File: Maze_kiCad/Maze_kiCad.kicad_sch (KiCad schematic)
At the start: 1 part, among them U1 ESP32-S2-DevKitC-1

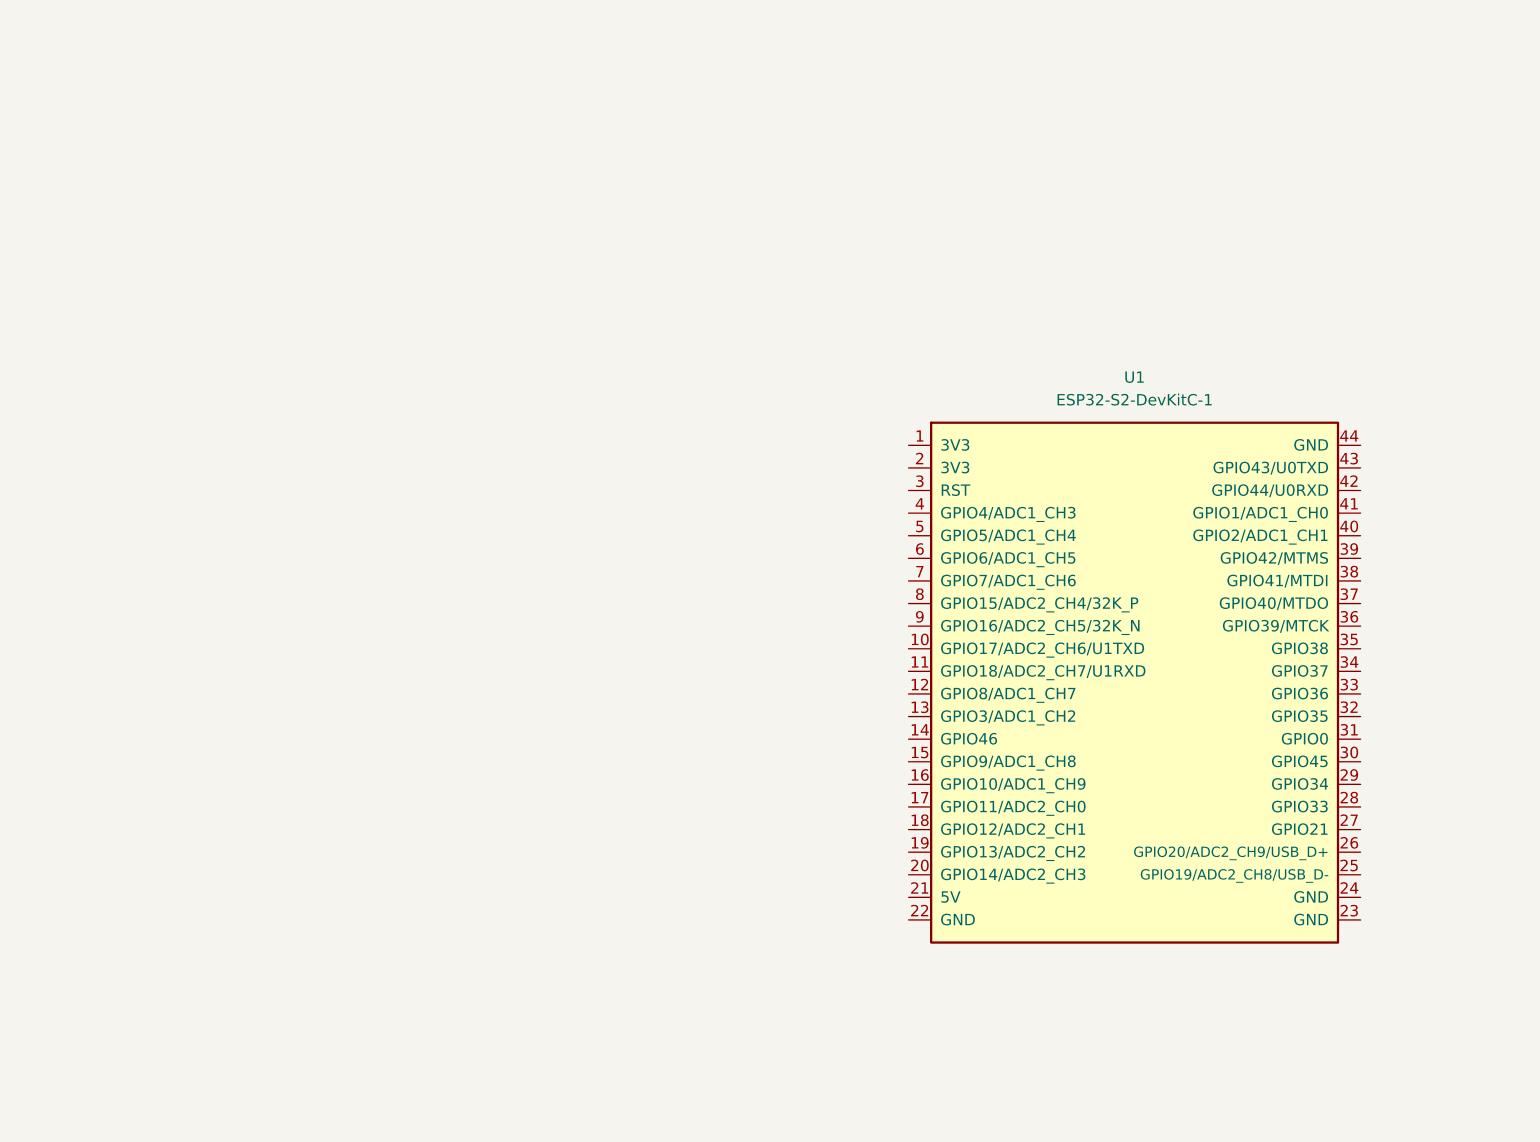
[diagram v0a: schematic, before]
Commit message: Add ir sensor
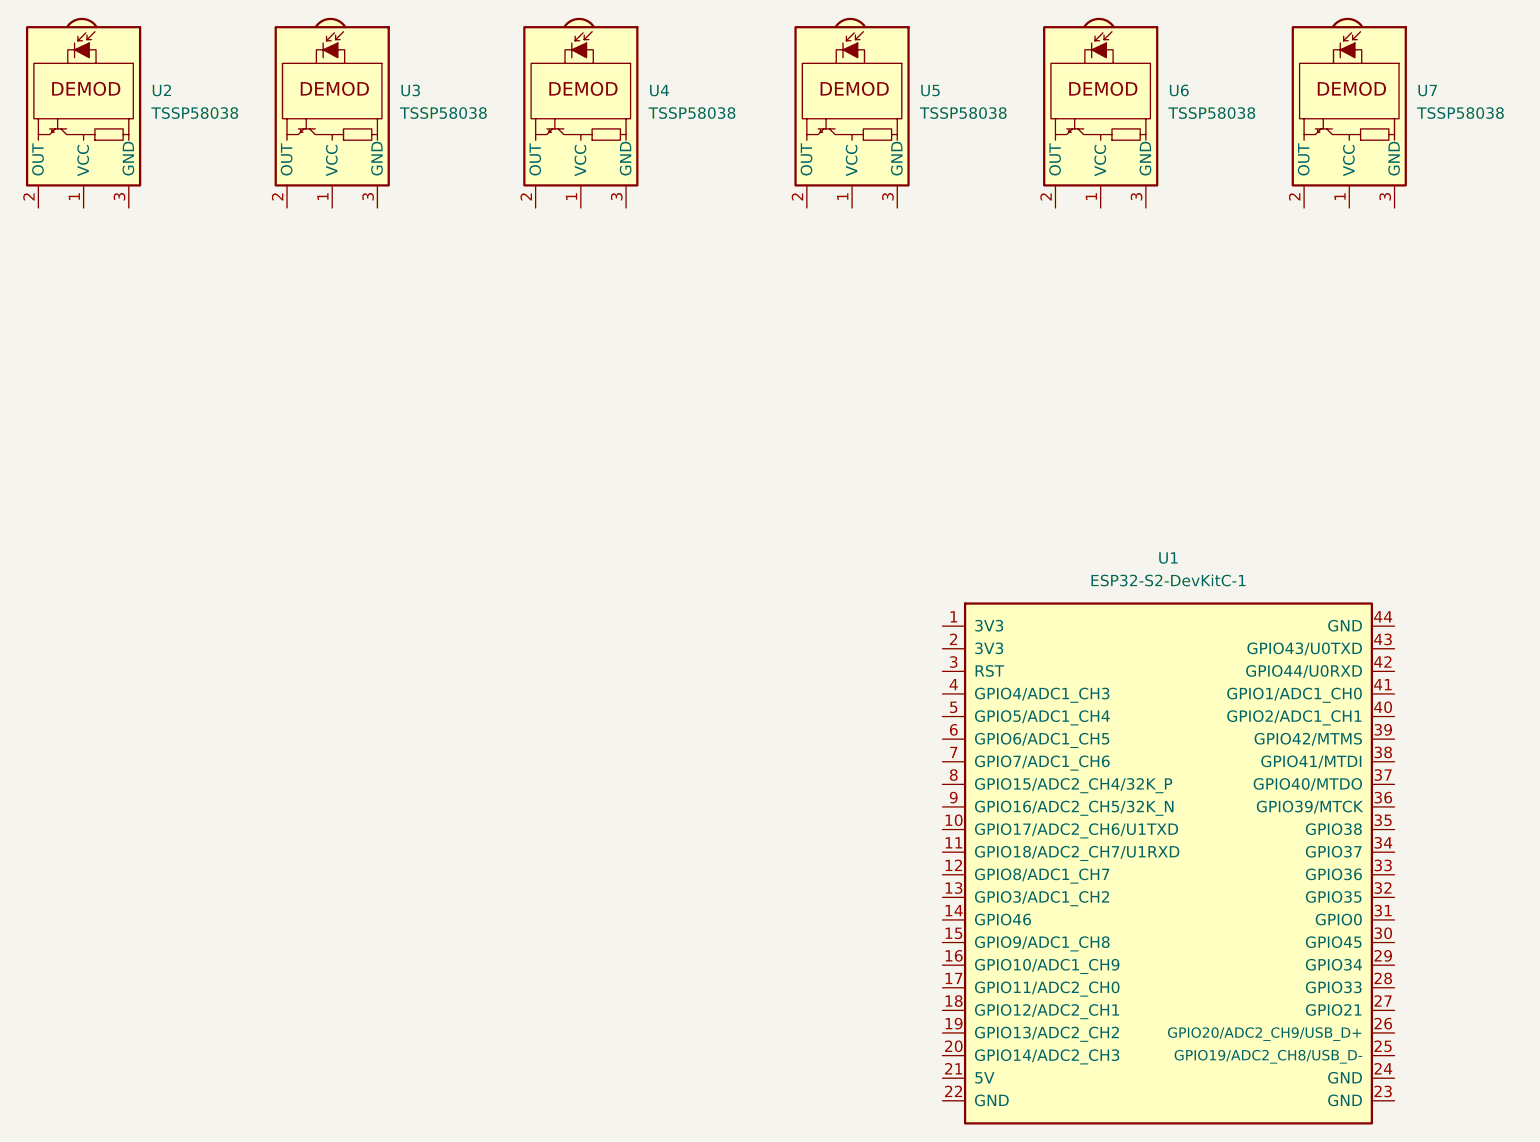
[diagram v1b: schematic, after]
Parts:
- added U2, U3, U4, U5, U6, U7: TSSP58038, OptoDevice:Vishay_MINICAST-3Pin, symbol Sensor_Proximity:TSSP58038
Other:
- moved on the sheet: U1

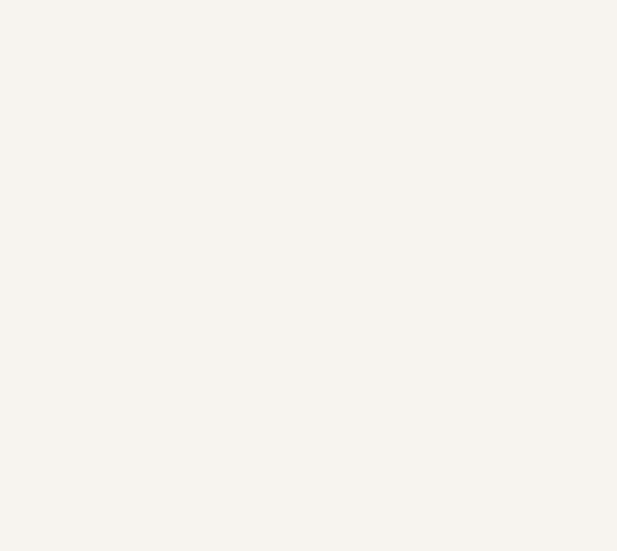
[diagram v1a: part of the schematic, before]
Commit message: add gyroscope symbol-footprint
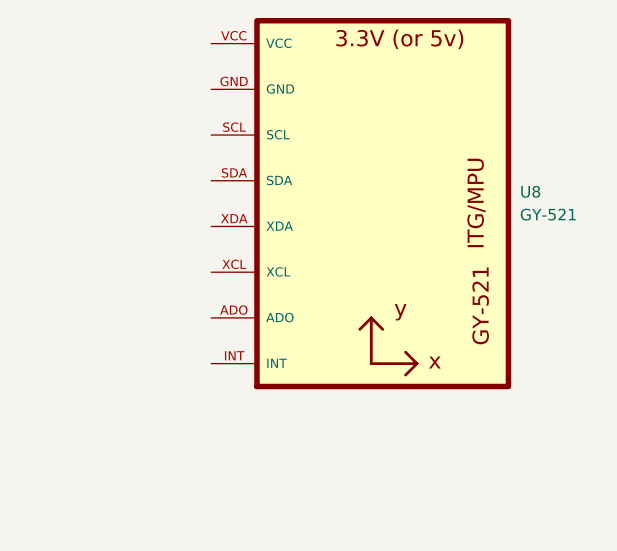
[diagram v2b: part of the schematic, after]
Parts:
- added U8: GY-521, mpu6050:GY-521, symbol mpu6050:GY-521
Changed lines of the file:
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@@
+	)
+	(symbol
+		(lib_id "mpu6050:GY-521")
+		(at 255.27 35.56 0)
+		(unit 1)
+		(exclude_from_sim no)
+		(in_bom yes)
+		(on_board yes)
+		(dnp no)
+		(fields_autoplaced yes)
+		(property "Reference" "U8"
+			(at 274.32 36.8299 0)
+			(effects
+				(font
+					(size 1.27 1.27)
+				)
+				(justify left)
+			)
+		)
+		(property "Value" "GY-521"
+			(at 274.32 39.3699 0)
+			(effects
+				(font
+					(size 1.27 1.27)
+				)
+				(justify left)
+			)
+		)
+		(property "Footprint" "mpu6050:GY-521"
+			(at 255.27 35.56 0)
+			(effects
+				(font
+					(size 1.27 1.27)
+				)
+				(justify bottom)
+				(hide yes)
+			)
+		)
+		(property "Datasheet" ""
+			(at 255.27 35.56 0)
+			(effects
+				(font
+					(size 1.27 1.27)
+				)
+				(hide yes)
+			)
+		)
+		(property "Description" ""
+			(at 255.27 35.56 0)
+			(effects
+				(font
+					(size 1.27 1.27)
+				)
+				(hide yes)
+			)
+		)
+		(property "MF" "GODREAM FORDREAM CO., LIMITED"
+			(at 255.27 35.56 0)
+			(effects
+				(font
+					(size 1.27 1.27)
+				)
+				(justify bottom)
+				(hide yes)
+			)
+		)
+		(property "Description_1" "\nTriple Axis Accelerometer Gyro Breakout\n"
+			(at 255.27 35.56 0)
+			(effects
+				(font
+					(size 1.27 1.27)
+				)
+				(justify bottom)
+				(hide yes)
+			)
+		)
+		(property "Package" "Package"
+			(at 255.27 35.56 0)
+			(effects
+				(font
+					(size 1.27 1.27)
+				)
+				(justify bottom)
+				(hide yes)
+			)
+		)
+		(property "Price" "None"
+			(at 255.27 35.56 0)
+			(effects
+				(font
+					(size 1.27 1.27)
+				)
+				(justify bottom)
+				(hide yes)
+			)
+		)
+		(property "SnapEDA_Link" "https://www.snapeda.com/parts/GY-521/GODREAM+FORDREAM+CO.%252C+LIMITED/view-part/?ref=snap"
+			(at 255.27 35.56 0)
+			(effects
+				(font
+					(size 1.27 1.27)
+				)
+				(justify bottom)
+				(hide yes)
+			)
+		)
+		(property "MP" "GY-521"
+			(at 255.27 35.56 0)
+			(effects
+				(font
+					(size 1.27 1.27)
+				)
+				(justify bottom)
+				(hide yes)
+			)
+		)
+		(property "Availability" "Not in stock"
+			(at 255.27 35.56 0)
+			(effects
+				(font
+					(size 1.27 1.27)
+				)
+				(justify bottom)
+				(hide yes)
+			)
+		)
+		(property "Check_prices" "https://www.snapeda.com/parts/GY-521/GODREAM+FORDREAM+CO.%252C+LIMITED/view-part/?ref=eda"
+			(at 255.27 35.56 0)
+			(effects
+				(font
+					(size 1.27 1.27)
+				)
+				(justify bottom)
+				(hide yes)
+			)
+		)
+		(pin "SCL"
+		)
+		(pin "INT"
+		)
+		(pin "XDA"
+		)
+		(pin "GND"
+		)
+		(pin "SDA"
+		)
+		(pin "XCL"
+		)
+		(pin "ADO"
+		)
+		(pin "VCC"
+		)
+		(instances
+			(project "Maze_kiCad"
+				(path "/22108416-3e7d-4108-b707-2b088264c2dd"
+					(reference "U8")
+					(unit 1)
+				)
+			)
+		)
 	)
 	(symbol

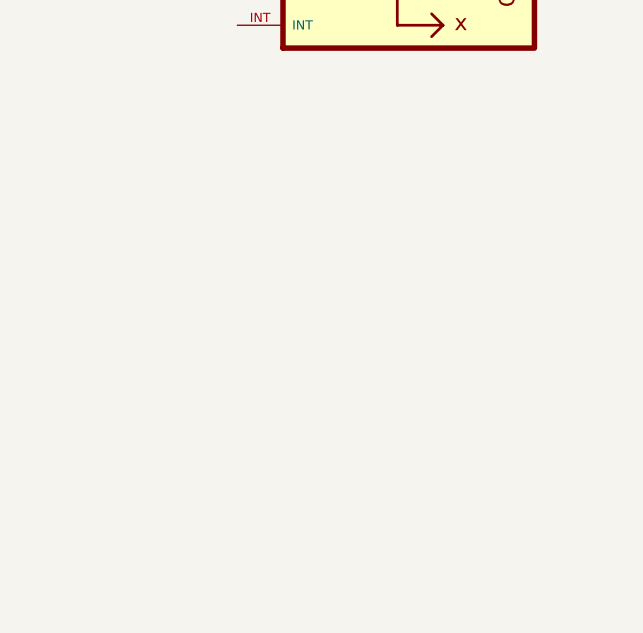
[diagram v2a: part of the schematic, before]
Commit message: drv8835 motor driver symnol and footprint
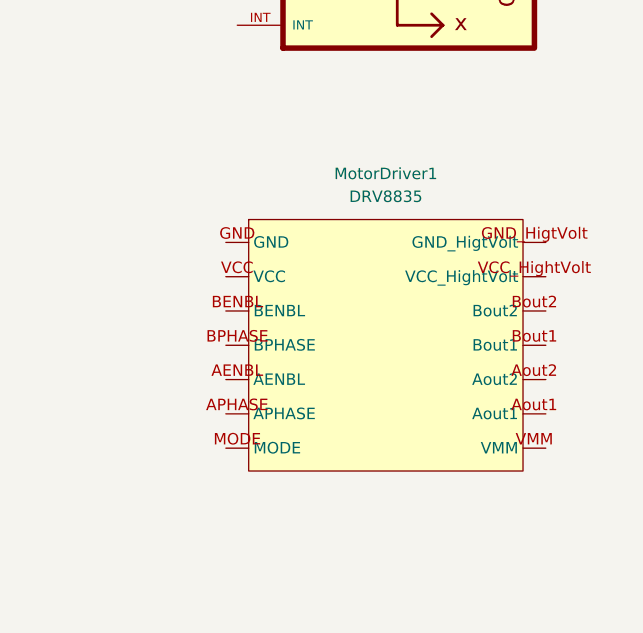
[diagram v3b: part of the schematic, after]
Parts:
- added MotorDriver1: DRV8835, drv8835:drv8835, symbol drv8835:DRV8835
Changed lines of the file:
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@@
+	)
+	(symbol
+		(lib_id "drv8835:DRV8835")
+		(at 284.48 69.85 0)
+		(unit 1)
+		(exclude_from_sim no)
+		(in_bom yes)
+		(on_board yes)
+		(dnp no)
+		(fields_autoplaced yes)
+		(property "Reference" "MotorDriver1"
+			(at 256.54 72.39 0)
+			(effects
+				(font
+					(size 1.27 1.27)
+				)
+			)
+		)
+		(property "Value" "DRV8835"
+			(at 256.54 74.93 0)
+			(effects
+				(font
+					(size 1.27 1.27)
+				)
+			)
+		)
+		(property "Footprint" "drv8835:drv8835"
+			(at 256.54 92.71 0)
+			(effects
+				(font
+					(size 1.27 1.27)
+				)
+				(hide yes)
+			)
+		)
+		(property "Datasheet" ""
+			(at 256.54 92.71 0)
+			(effects
+				(font
+					(size 1.27 1.27)
+				)
+				(hide yes)
+			)
+		)
+		(property "Description" ""
+			(at 256.54 92.71 0)
+			(effects
+				(font
+					(size 1.27 1.27)
+				)
+				(hide yes)
+			)
+		)
+		(pin "BENBL"
+		)
+		(pin "AENBL"
+		)
+		(pin "APHASE"
+		)
+		(pin "VMM"
+		)
+		(pin "BPHASE"
+		)
+		(pin "Aout1"
+		)
+		(pin "Aout2"
+		)
+		(pin "GND_HigtVolt"
+		)
+		(pin "Bout1"
+		)
+		(pin "GND"
+		)
+		(pin "MODE"
+		)
+		(pin "VCC_HightVolt"
+		)
+		(pin "VCC"
+		)
+		(pin "Bout2"
+		)
+		(instances
+			(project "Maze_kiCad"
+				(path "/22108416-3e7d-4108-b707-2b088264c2dd"
+					(reference "MotorDriver1")
+					(unit 1)
+				)
+			)
+		)
 	)
 	(symbol
